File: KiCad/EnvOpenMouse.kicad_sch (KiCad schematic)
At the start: 68 parts, among them J2 Button, J3 Conn_01x05, J4 Conn_01x09, J5 Conn_02x02_Top_Bottom, J5 SKRKAEE020, J6 Conn_02x02_Top_Bottom, J7 Conn_02x02_Top_Bottom, J8 Conn_02x02_Top_Bottom, J9 Conn_01x03, SW1 SW_Push_SPDT, SW2 SW_Push_SPDT, SW3 SW_Push_SPDT, U1 TLV75733PDBVR, U2 TLV70218DBVR, U3 BQ24074RGT, U3 RP2040, U4 PMW3360DM-T2QU, Y1 3225_4P 12MHz

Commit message: corrected some issues and updated gerbers
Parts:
- removed U1: TLV75733PDBVR, Package_SON:WSON-6-1EP_2x2mm_P0.65mm_EP1x1.6mm, symbol Regulator_Linear:TLV75733PDRV
- added U1: AP2112K-3.3, Package_TO_SOT_SMD:SOT-23-5, symbol Regulator_Linear:AP2112K-3.3
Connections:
- net +3V3: now also U1.5 (VOUT)
- net GND: now also U1.2 (GND)
- net VDD: now also U1.1 (VIN)
- net at R4.2: now also U1.3 (EN)
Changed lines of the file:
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@@
-    )
-  )
-  (symbol (lib_id "Regulator_Linear:TLV75733PDRV") (at 255.905 33.655 0) (unit 1)
-    (in_bom yes) (on_board yes) (dnp no) (fields_autoplaced)
-    (property "Reference" "U1" (at 255.905 24.765 0)
-      (effects (font (size 1.27 1.27)))
-    )
-    (property "Value" "TLV75733PDBVR" (at 255.905 27.305 0)
-      (effects (font (size 1.27 1.27)))
-    )
-    (property "Footprint" "Package_SON:WSON-6-1EP_2x2mm_P0.65mm_EP1x1.6mm" (at 255.905 25.4 0)
-      (effects (font (size 1.27 1.27) italic) hide)
-    )
-    (property "Datasheet" "https://www.ti.com/lit/ds/symlink/tlv757p.pdf" (at 255.905 32.385 0)
-      (effects (font (size 1.27 1.27)) hide)
-    )
-    (pin "1")
-    (pin "2")
-    (pin "3")
-    (pin "4")
-    (pin "5")
-    (pin "6")
-    (pin "7")
-    (instances
-      (project "EnvOpenMouse"
-        (path "/8ba470d4-e08f-44d0-a74b-2d70d975113e"
-          (reference "U1") (unit 1)
-        )
-      )
     )
   )
@@
         )
       )
+    )
+  )
+  (symbol (lib_id "Regulator_Linear:AP2112K-3.3") (at 255.905 33.655 0) (unit 1)
+    (in_bom yes) (on_board yes) (dnp no) (fields_autoplaced)
+    (property "Reference" "U1" (at 255.905 25.4 0)
+      (effects (font (size 1.27 1.27)))
+    )
+    (property "Value" "AP2112K-3.3" (at 255.905 27.94 0)
+      (effects (font (size 1.27 1.27)))
+    )
+    (property "Footprint" "Package_TO_SOT_SMD:SOT-23-5" (at 255.905 25.4 0)
+      (effects (font (size 1.27 1.27)) hide)
+    )
+    (property "Datasheet" "https://www.diodes.com/assets/Datasheets/AP2112.pdf" (at 255.905 31.115 0)
+      (effects (font (size 1.27 1.27)) hide)
+    )
+    (pin "1")
+    (pin "2")
+    (pin "3")
+    (pin "4")
+    (pin "5")
+    (instances
+      (project "EnvOpenMouse"
+        (path "/8ba470d4-e08f-44d0-a74b-2d70d975113e"
+          (reference "U1") (unit 1)
+        )
+      )

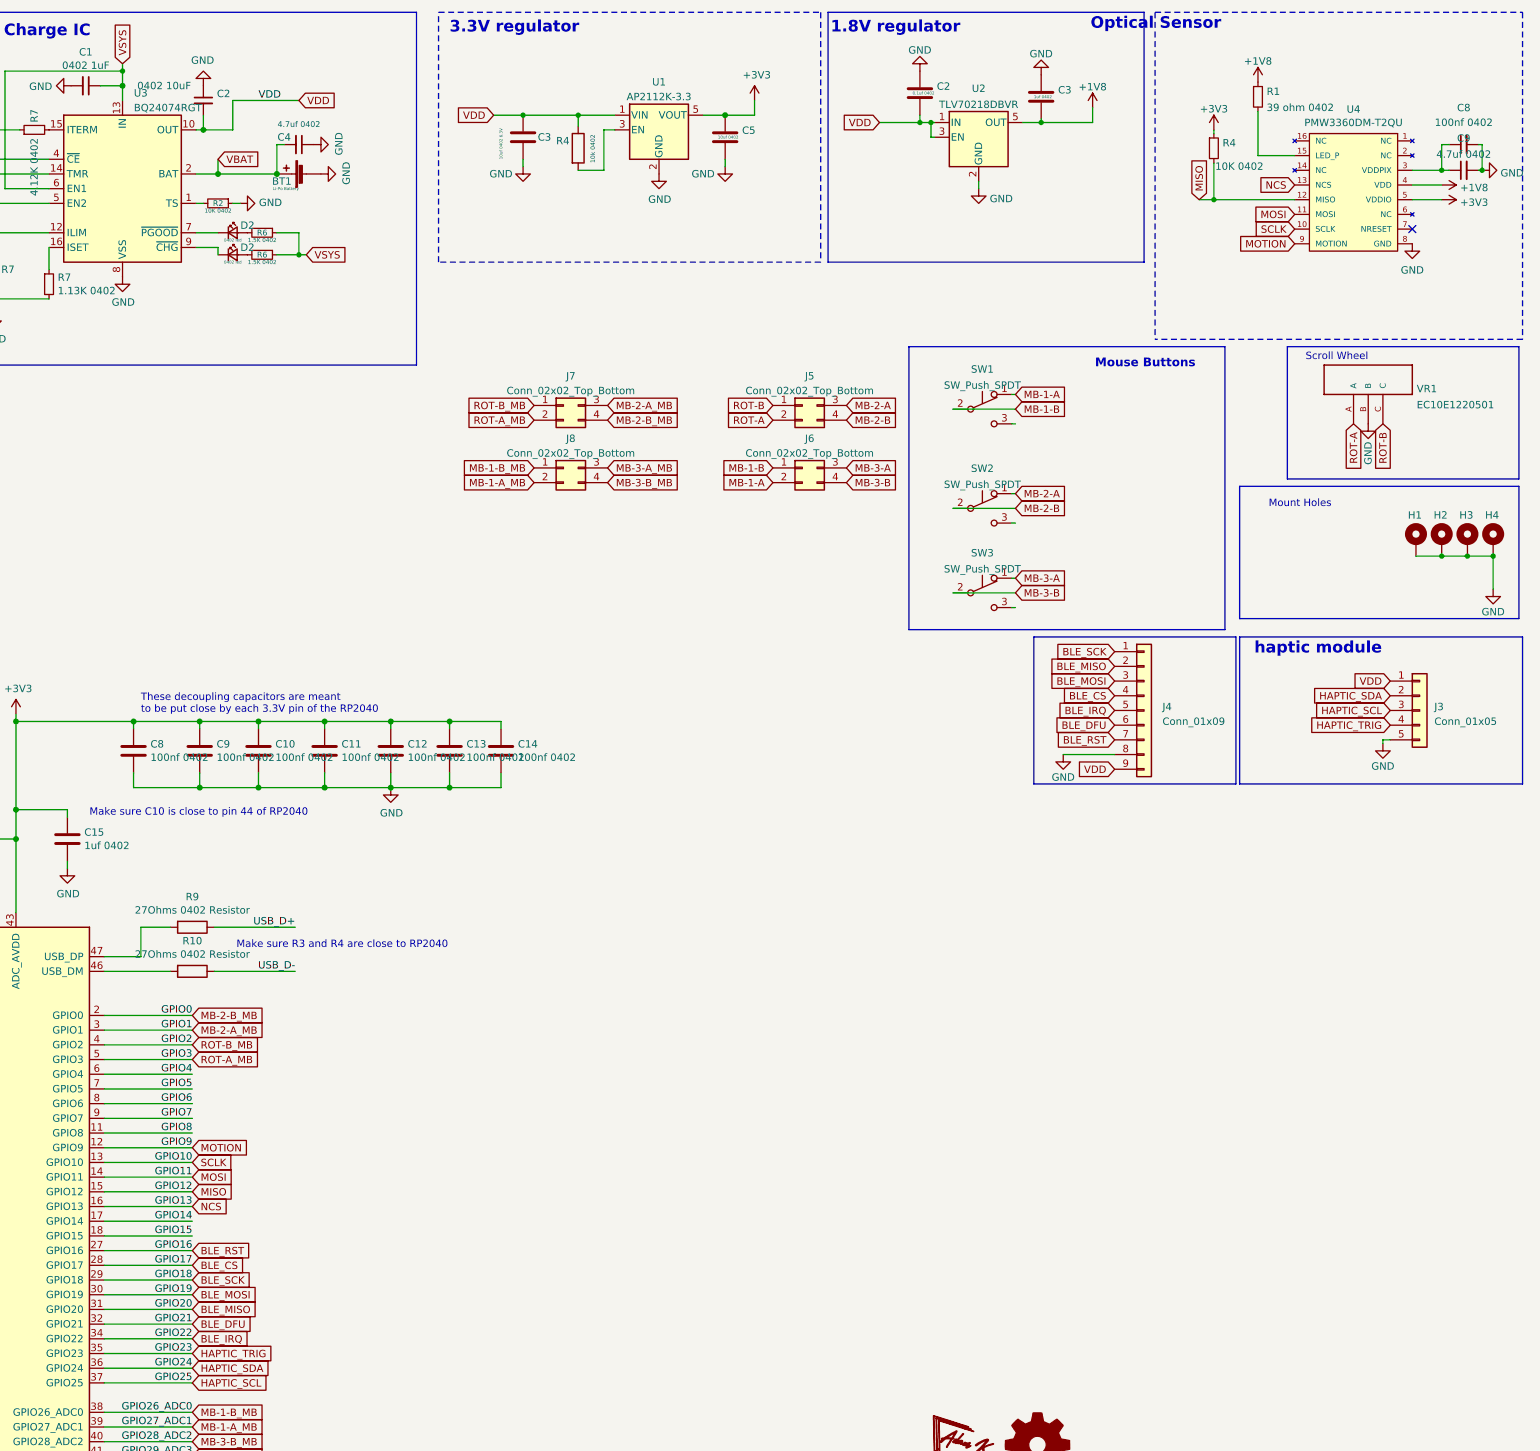
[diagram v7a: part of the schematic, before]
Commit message: corrected some issues with the design + added  fpc/ffc for cirque glidepoint
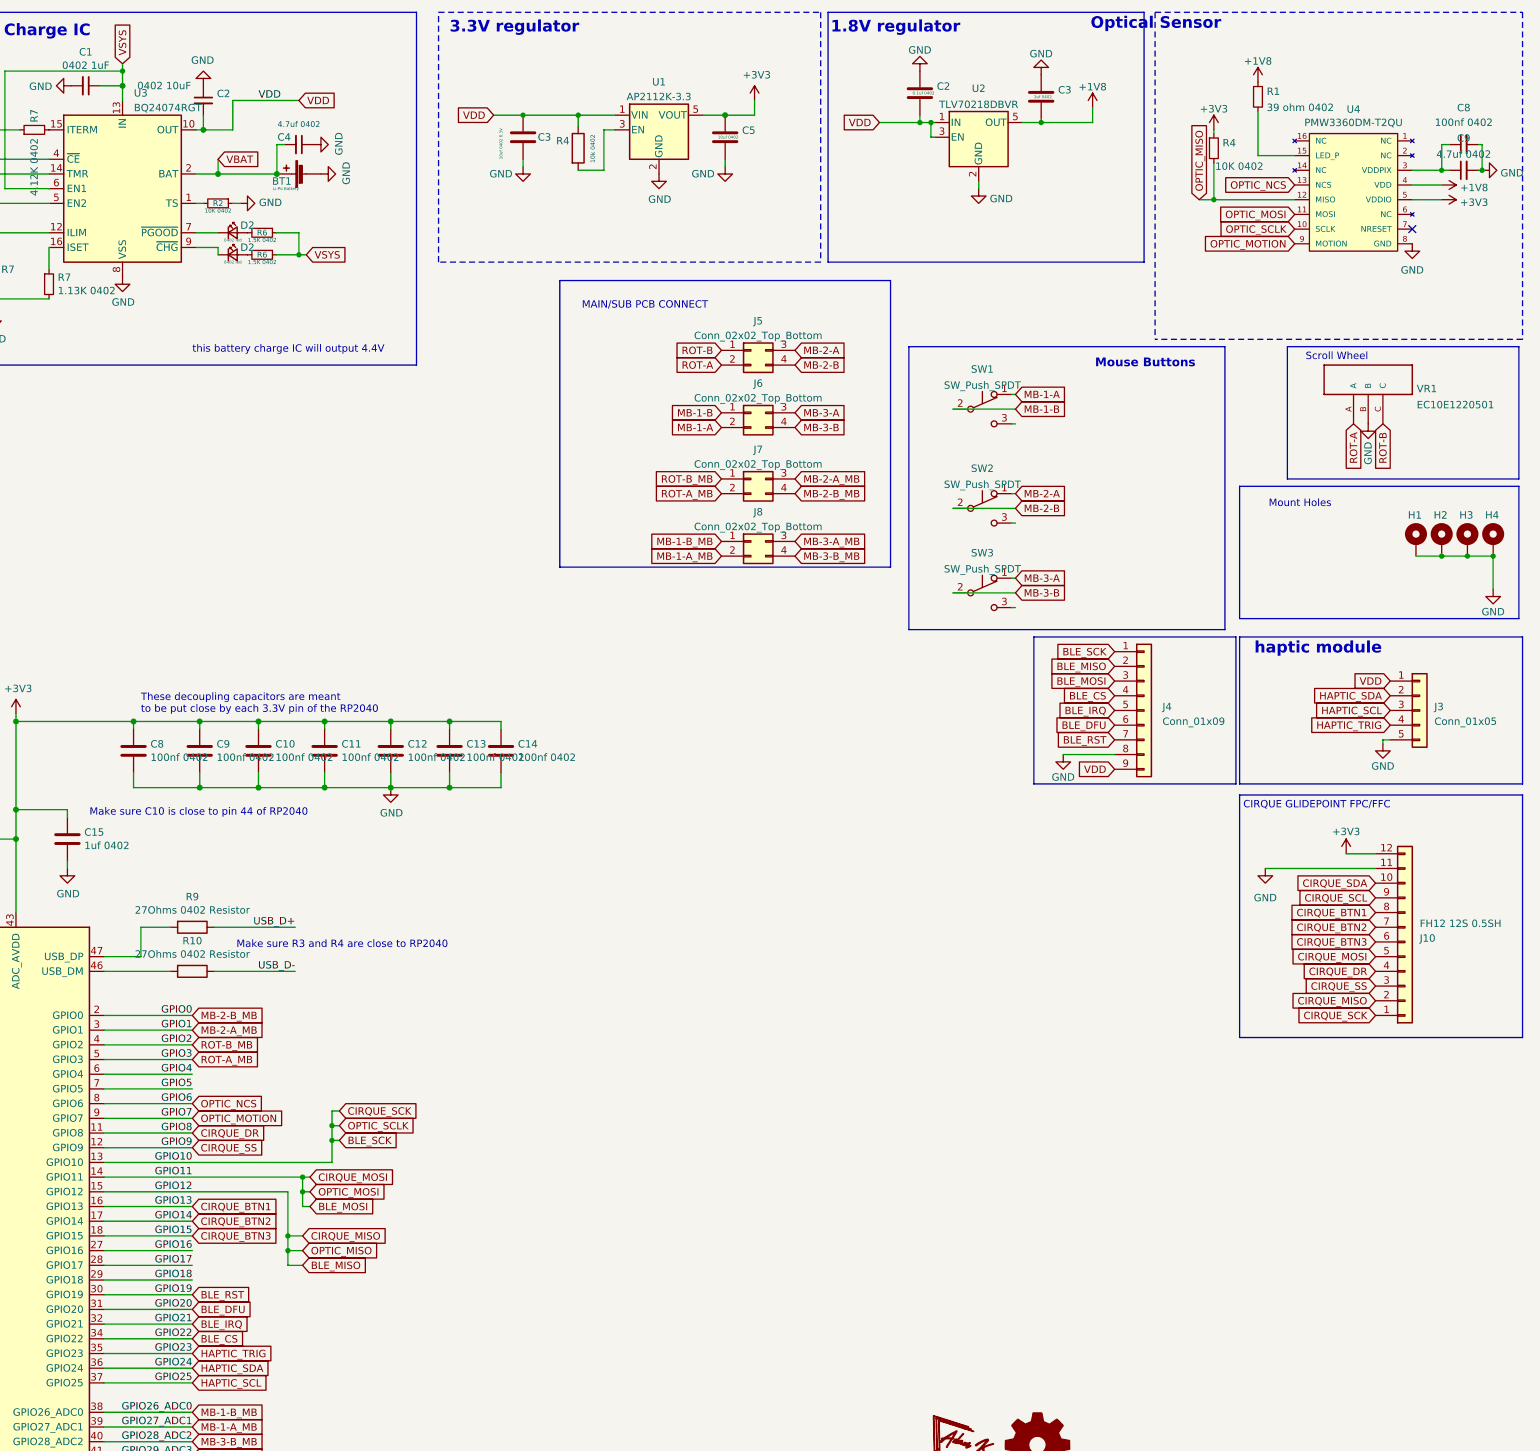
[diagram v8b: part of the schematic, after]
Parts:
- added J10: FH12 12S 0.5SH, Connector_FFC-FPC:Hirose_FH12-12S-0.5SH_1x12-1MP_P0.50mm_Horizontal, symbol Connector_Generic:Conn_01x12
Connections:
- net MISO is gone; now on net BLE_MISO: R4.2, U3.15 (GPIO12), U4.12 (MISO)
- net MOSI is gone; now on net BLE_MOSI: U3.14 (GPIO11), U4.11 (MOSI)
- net SCLK is gone; now on net BLE_SCK: U3.13 (GPIO10), U4.10 (SCLK)
- net +3V3: now also J10.12 (Pin_12)
- net BLE_CS: now also U3.34 (GPIO22); no longer U3.28 (GPIO17)
- net BLE_DFU: now also U3.31 (GPIO20); no longer U3.32 (GPIO21)
- net BLE_IRQ: now also U3.32 (GPIO21); no longer U3.34 (GPIO22)
- net BLE_MISO: now also J10.2 (Pin_2); no longer U3.31 (GPIO20)
- net BLE_MOSI: now also J10.5 (Pin_5); no longer U3.30 (GPIO19)
- net BLE_RST: now also U3.30 (GPIO19); no longer U3.27 (GPIO16)
- net BLE_SCK: now also J10.1 (Pin_1); no longer U3.29 (GPIO18)
- net GND: now also J10.11 (Pin_11)
- net GPIO14 renamed CIRQUE_BTN2
- net CIRQUE_BTN2: now also J10.7 (Pin_7)
- net GPIO15 renamed CIRQUE_BTN3
- net CIRQUE_BTN3: now also J10.6 (Pin_6)
- net GPIO6 renamed OPTIC_NCS
- net OPTIC_NCS: now also U4.13 (NCS)
- net GPIO7 renamed OPTIC_MOTION
- net OPTIC_MOTION: now also U4.9 (MOTION)
- net GPIO8 renamed CIRQUE_DR
- net CIRQUE_DR: now also J10.4 (Pin_4)
- net MOTION renamed CIRQUE_SS
- net CIRQUE_SS: now also J10.3 (Pin_3); no longer U4.9 (MOTION)
- net NCS renamed CIRQUE_BTN1
- net CIRQUE_BTN1: now also J10.8 (Pin_8); no longer U4.13 (NCS)
- new net CIRQUE_SCL: J10.9 (Pin_9)
- new net CIRQUE_SDA: J10.10 (Pin_10)
- new net GPIO16: U3.27 (GPIO16)
- new net GPIO17: U3.28 (GPIO17)
- new net GPIO18: U3.29 (GPIO18)
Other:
- note added: "CIRQUE GLIDEPOINT FPC/FFC"
- note added: "MAIN/SUB PCB CONNECT"
- note added: "this battery charge IC will output 4.4V"
- moved on the sheet: J5, J6, J7, J8
